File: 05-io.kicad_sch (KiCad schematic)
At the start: 34 parts, among them J6 GPS_unbestueckt, J7 I2C_Erweiterung, Q3 2N7002, Q4 2N7002, SW3 REC, SW4 MARK, U7 DS3231SN, U8 SN65HVD230D

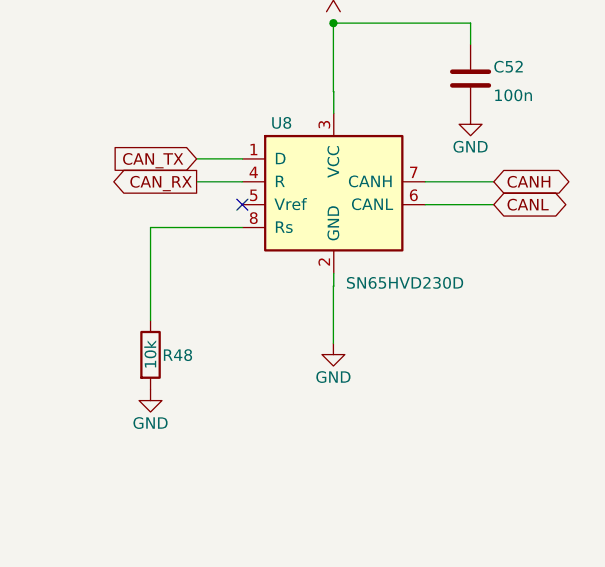
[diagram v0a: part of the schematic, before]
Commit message: Werte der Ersatztypen nachziehen und Felder auf die Platine uebertragen
Vier Bauteile trugen nach dem Ersatz einen Wert, der nicht mehr zum
eingebauten Typ passte: U2 (NCP1117ST33), U3 (LP5907MFX-3.3), U8
(SN65HVD230Q) und Q1 (SI2309CDS). Die uebrigen fuenf Ersatztypen behalten
ihren Wert - LM5164DDA, 24.576MHz, BZX84C15, PMEG3020 und OPA2325 sind
Typbezeichnungen, die auch fuer die Ersatznummer gelten.

Die Beschaffungsfelder standen bisher nur im Schaltplan. KiCads Abgleich
vergleicht auch Felder und meldete darum fuer fast jedes Bauteil eine
Abweichung - 144 statt vorher 8. tools/sync_pcb_fields.py traegt Wert und
Felder aus der Netzliste in die Bauteile auf der Platine nach, unsichtbar
und auf der Fabrikationslage. Danach bleiben 18 Abweichungen auf der
Hauptplatine und 2 auf dem Mikrofonkopf, alle aelteren Datums: der
Schaltplan auf der Platte kennt Footprints, die so nicht baubar sind
(Superseal auf der Platine, TSSOP-30 mit falschem Raster, ESP32-S2-Modul),
das Layout hat sie laengst ersetzt.

Nebenbei zwei Fehler in der eigenen Pruefung behoben, die erst jetzt
auffielen: der Kantenabstand wurde gegen den Ursprung gerechnet, obwohl
KiCad die Kontur beim Bearbeiten auf die Blattmitte geschoben hat
(117/70 statt 0/0) - das ergab 2914 Scheinbeanstandungen. Und
PCB_VIA::GetWidth() will in KiCad 10 die Lage wissen.

DRC unveraendert: 0 Fehler, 10 Warnungen, 7 offene Verbindungen.
Stuecklisten, Fertigungsdaten und Schaltplan-PDFs neu erzeugt.
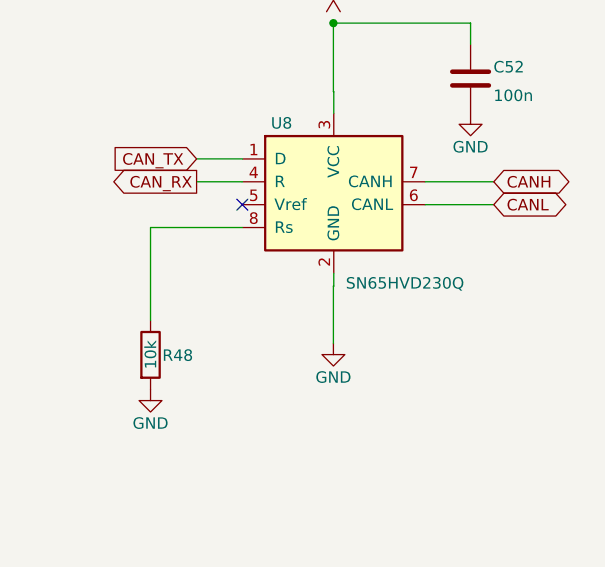
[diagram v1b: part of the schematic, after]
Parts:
- U8: value SN65HVD230D -> SN65HVD230Q
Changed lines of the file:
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@@
 			)
 		)
-		(property "Value" "SN65HVD230D"
+		(property "Value" "SN65HVD230Q"
 			(at 327.954 81.13 0)
 			(show_name no)

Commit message: Footprints im Schaltplan auf den Stand des Layouts ziehen
Neun Bauteile trugen im Schaltplan einen Footprint, der so nicht baubar ist.
Das Layout hatte sie laengst ersetzt; jetzt steht es auch im Schaltplan:

  U5      TSSOP-30 4,4 x 9,7 / 0,65  ->  4,4 x 7,8 / 0,5  (Datenblatt)
  U6      ESP32-S2-WROOM             ->  ESP32-S3-WROOM-1
  L2, L3  L_CommonModeChoke_WE-SL2   ->  L_CommonMode_WE-SL2
  J1..J3  TE Superseal 1.0           ->  JST XH liegend
  BT1     Keystone 3034 / CR2032     ->  Keystone 3000 / CR1220
  LS1     Piezo bedrahtet 12 mm      ->  Murata-Landmuster 9 x 9 mm SMD

Wo sich damit das Bauteil aendert, sind Wert und Bestellnummer mitgezogen.
Zwei Punkte dabei zum Nachlesen:

* BT1 hat mit CR1220 rund ein Viertel der Kapazitaet von CR2032. Die
  Platine ist fuer den 12-mm-Halter gebohrt, darum folgt der Schaltplan.
* Der im Layout benannte Murata PKMCS0909E ist abgekuendigt ("Last Time
  Buy") und nur fuer 1,5 V spezifiziert, angesteuert wird aber mit 3,3 V.
  Bestellt wird darum ein 3-V-Typ gleicher Bauform (Same Sky
  CPT-9019A-SMT-TR); das Landmuster gehoert gegen das Datenblatt geprueft.

Damit sind die Steckverbinder J1..J3 beschaffbar - Superseal 1.0 gibt es bei
DigiKey nur kabelseitig. Offen bleiben noch J4 und MK1.

Schaltplanparitaet: 18 -> 9 Abweichungen auf der Hauptplatine, 2 auf dem
Mikrofonkopf. Die restlichen sind keine Footprints mehr, sondern Symbole:
U2 hat einen Pin 4, den das SOT-223 nicht hat, und dem microSD-Symbol fehlt
der Schirmanschluss. Beides steht im README.

Die Stueckliste fuehrt jetzt eine Spalte Hinweis - dort landen die
Ersatzgruende, die vorher nur im Schaltplan standen.

DRC unveraendert: 0 Fehler, 10 Warnungen, 7 offene Verbindungen. ERC
unveraendert. Stuecklisten, Fertigungsdaten und PDFs neu erzeugt.
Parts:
- BT1: value CR2032 -> CR1220; footprint Battery:BatteryHolder_Keystone_3034_1x20mm -> Battery:BatteryHolder_Keystone_3000_1x12mm; DigiKey 36-3034CT-ND -> 36-3000CT-ND; Hinweis (none) -> Layout traegt den 12-mm-Halter; CR1220 hat rund ein Viertel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; MPN 3034TR -> 3000TR
- LS1: value Piezo -> Piezo_9x9_SMD; footprint Buzzer_Beeper:Buzzer_12x9.5RM7.6 -> Buzzer_Beeper:Buzzer_Murata_PKMCS0909E; DigiKey 668-AT-1240-TT-ND -> 2223-CPT-9019A-SMT-TRCT-ND; Hersteller PUI Audio, Inc. -> Same Sky (Formerly CUI Devices); Hinweis (none) -> Landmuster aus der Murata-Bibliothek; Murata PKMCS0909E ist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; MPN AT-1240-TT -> CPT-9019A-SMT-TR
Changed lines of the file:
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@@
 			)
 		)
-		(property "Value" "Piezo"
+		(property "Value" "Piezo_9x9_SMD"
 			(at 322.58 203.835 0)
 			(show_name no)
@@
 			)
 		)
-		(property "Footprint" "Buzzer_Beeper:Buzzer_12x9.5RM7.6"
+		(property "Footprint" "Buzzer_Beeper:Buzzer_Murata_PKMCS0909E"
 			(at 317.5 201.93 0)
 			(hide yes)
@@
 			)
 		)
-		(property "MPN" "AT-1240-TT"
+		(property "MPN" "CPT-9019A-SMT-TR"
 			(at 317.5 201.93 0)
 			(hide yes)
@@
 			)
 		)
-		(property "Hersteller" "PUI Audio, Inc."
+		(property "Hersteller" "Same Sky (Formerly CUI Devices)"
 			(at 317.5 201.93 0)
 			(hide yes)
@@
 			)
 		)
-		(property "DigiKey" "668-AT-1240-TT-ND"
+		(property "DigiKey" "2223-CPT-9019A-SMT-TRCT-ND"
+			(at 317.5 201.93 0)
+			(hide yes)
+			(show_name no)
+			(do_not_autoplace no)
+			(effects
+				(font
+					(size 1.27 1.27)
+				)
+			)
+		)
+		(property "Hinweis" "Landmuster aus der Murata-Bibliothek; Murata PKMCS0909E ist abgekuendigt und nur fuer 1,5 V, darum ein 3-V-Typ gleicher Bauform - Landmuster gegen Datenblatt pruefen"
 			(at 317.5 201.93 0)
 			(hide yes)
@@
 			)
 		)
-		(property "Value" "CR2032"
+		(property "Value" "CR1220"
 			(at 142.24 70.485 0)
 			(show_name no)
@@
 			)
 		)
-		(property "Footprint" "Battery:BatteryHolder_Keystone_3034_1x20mm"
+		(property "Footprint" "Battery:BatteryHolder_Keystone_3000_1x12mm"
 			(at 139.7 68.58 0)
 			(hide yes)
@@
 			)
 		)
-		(property "MPN" "3034TR"
+		(property "MPN" "3000TR"
 			(at 139.7 68.58 0)
 			(hide yes)
@@
 			)
 		)
-		(property "DigiKey" "36-3034CT-ND"
+		(property "DigiKey" "36-3000CT-ND"
 			(at 139.7 68.58 0)
 			(hide yes)
+			(show_name no)
+			(do_not_autoplace no)
+			(effects
+				(font
+					(size 1.27 1.27)
+				)
+			)
+		)
+		(property "Hinweis" "Layout traegt den 12-mm-Halter; CR1220 hat rund ein Viertel der Kapazitaet von CR2032"
+			(at 139.7 68.58 0)
+			(hide yes)

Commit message: Fehlende PWR_FLAG setzen - ERC auf beiden Platinen fehlerfrei
KiCad prueft, ob jedes Versorgungsnetz von einem Ausgang gespeist wird. An
fuenf Netzen sitzt keine Quelle, die es als solche erkennt: +4V6, AVDD
(U5 Pin 14 des ADC-Reglers ueber die Ferritperle) und VBAT (U7 Pin 14, aus
der Knopfzelle) auf der Hauptplatine, dazu Reglereingang und Masse beim
Mikrofonkopf, die beide ueber das Kabel hereinkommen. Ein PWR_FLAG sagt dem
ERC, dass das Absicht ist; an der Schaltung aendert es nichts.

tools/add_pwr_flags.py schreibt die Bloecke von vorhandenen Symbolen ab und
verschiebt sie, damit Aufbau und Schreibweise zur Datei passen - neue UUIDs,
freie Referenzen, Blattpfad je Blatt, und beim Mikrofonkopf der flache Pfad
seines eigenen Projekts. Die Zapfpunkte sind so gewaehlt, dass Flagge und
Draht keine vorhandene Grafik ueberdecken.

ERC: 3 -> 0 Fehler auf der Hauptplatine, 2 -> 0 auf dem Mikrofonkopf.
Einziger Nebeneffekt sind fuenf weitere endpoint_off_grid-Warnungen; davon
gab es schon 252, weil der Generator das ganze Blatt auf ein feineres
Raster als 1,27 mm gesetzt hat.

DRC unveraendert: 0 Fehler, 10 Warnungen, 7 offene Verbindungen.
Schaltplanparitaet unveraendert bei 4 beziehungsweise 2 - nur die
Befestigungsbohrungen. Stuecklisten, Fertigungsdaten und PDFs neu erzeugt.
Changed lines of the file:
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@@
+	)
+	(symbol
+		(lib_id "power:PWR_FLAG")
+		(at 107.95 57.15 0)
+		(unit 1)
+		(body_style 1)
+		(exclude_from_sim no)
+		(in_bom no)
+		(on_board yes)
+		(in_pos_files yes)
+		(dnp no)
+		(property "Reference" "#FLG0005"
+			(at 110.49 55.88 0)
+			(show_name no)
+			(do_not_autoplace no)
+			(effects
+				(font
+					(size 1.27 1.27)
+				)
+				(justify left)
+			)
+		)
+		(property "Value" "PWR_FLAG"
+			(at 110.49 59.055 0)
+			(show_name no)
+			(do_not_autoplace no)
+			(effects
+				(font
+					(size 1.27 1.27)
+				)
+				(justify left)
+			)
+		)
+		(property "Footprint" ""
+			(at 107.95 57.15 0)
+			(hide yes)
+			(show_name no)
+			(do_not_autoplace no)
+			(effects
+				(font
+					(size 0.508 0.508)
+				)
+			)
+		)
+		(property "Datasheet" ""
+			(at 107.95 57.15 0)
+			(hide yes)
+			(show_name no)
+			(do_not_autoplace no)
+			(effects
+				(font
+					(size 1.27 1.27)
+				)
+			)
+		)
+		(property "Description" ""
+			(at 107.95 57.15 0)
+			(show_name no)
+			(do_not_autoplace no)
+			(effects
+				(font
+					(size 1.27 1.27)
+				)
+			)
+		)
+		(pin "1"
+		)
+		(instances
+			(project "exhaust-mic"
+				(path "/24901e4d-8246-6c3d-a980-c1f8cf14e631/5a04efcd-e24a-0d89-f2fd-e1fa0e6e92cb"
+					(reference "#FLG0005")
+					(unit 1)
+				)
+			)
+		)
+	)
+	(wire
+		(pts
+			(xy 107.95 57.15) (xy 107.95 63.5)
+		)
+		(stroke
+			(width 0)
+			(type default)
+		)
+	)
+	(junction
+		(at 107.95 63.5)
+		(diameter 0)
+		(color 0 0 0 0)
 	)
 	(symbol
